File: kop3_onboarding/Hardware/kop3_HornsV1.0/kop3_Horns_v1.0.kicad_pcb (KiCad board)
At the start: 2 copper layers, 0 parts

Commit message: PCB Layout for Horn Breakout Board Done.
Created the PCB for the Horn Breakout Board.
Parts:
- added C1: 100 uF, Capacitor_SMD:C_0805_2012Metric_Pad1.18x1.45mm_HandSolder, F.Cu at (75.5, 63.0)
- added C10: C, Capacitor_SMD:C_0805_2012Metric_Pad1.18x1.45mm_HandSolder, F.Cu at (75.5, 44.9)
- added C11: .01 uF, Capacitor_SMD:C_0805_2012Metric_Pad1.18x1.45mm_HandSolder, F.Cu at (75.5, 41.9)
- added C12: .01 uF, Capacitor_SMD:C_0805_2012Metric_Pad1.18x1.45mm_HandSolder, F.Cu at (75.5, 38.9)
- added C2: .01 uF, Capacitor_SMD:C_0805_2012Metric_Pad1.18x1.45mm_HandSolder, F.Cu at (75.5, 60.0)
- added C4: 10 uF, Capacitor_SMD:C_0805_2012Metric_Pad1.18x1.45mm_HandSolder, F.Cu at (75.5, 57.0)
- added C5: 10 uF, Capacitor_SMD:C_0805_2012Metric_Pad1.18x1.45mm_HandSolder, F.Cu at (75.5, 54.0)
- added C6: 1 uF, Capacitor_SMD:C_0805_2012Metric_Pad1.18x1.45mm_HandSolder, F.Cu at (75.5, 51.0)
- added C7: 1 uF, Capacitor_SMD:C_0805_2012Metric_Pad1.18x1.45mm_HandSolder, F.Cu at (75.5, 48.0)
- added D2: S2JTR, Diode_SMD:D_SMB, F.Cu at (99.0, 53.8)
- added F1: 2A, Fuse:Fuse_0805_2012Metric_Pad1.15x1.40mm_HandSolder, F.Cu at (100.2, 47.5)
- added J1: Power, Connector_Molex:Molex_KK-254_AE-6410-03A_1x03_P2.54mm_Vertical, F.Cu at (86.8, 63.3)
- added J2: HORN_CONTROL, Connector_Molex:Molex_KK-254_AE-6410-02A_1x02_P2.54mm_Vertical, F.Cu at (81.7, 40.8)
- added J3: HORN_OUT1, Connector_Molex:Molex_KK-254_AE-6410-02A_1x02_P2.54mm_Vertical, F.Cu at (89.5, 40.8)
- added J4: HORN_OUT2, Connector_Molex:Molex_KK-254_AE-6410-02A_1x02_P2.54mm_Vertical, F.Cu at (96.5, 40.8)
- added Q1: IRF540N, Package_TO_SOT_THT:TO-220-3_Vertical, F.Cu at (93.0, 51.3)
- added R1: 1K, Resistor_THT:R_Axial_DIN0204_L3.6mm_D1.6mm_P5.08mm_Horizontal, F.Cu at (83.0, 54.0)
- added REF**: MountingHole_3.2mm_M3, MountingHole:MountingHole_3.2mm_M3, F.Cu at (99.8, 70.2)
- added REF**: MountingHole_3.2mm_M3, MountingHole:MountingHole_3.2mm_M3, F.Cu at (77.0, 32.5)
- added SW1: SW_Push, Button_Switch_SMD:SW_Push_1P1T_NO_6x6mm_H9.5mm, F.Cu at (96.3, 61.8)
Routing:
- net GND: track 0.00 -> 47.8 mm, vias 0 -> 1
- net +24V: track 0.00 -> 37.2 mm
- net /HORN_CONTROL: track 0.00 -> 30.5 mm
- net Net-(D2-K): track 0.00 -> 21.2 mm
- net Net-(J4-Pin_2): track 0.00 -> 6.21 mm
- net Net-(J3-Pin_2): track 0.00 -> 4.45 mm
- net Net-(D2-A): track 0.00 -> 3.59 mm
- added copper zone on F.Cu, net +24V
- added copper zone on B.Cu, net GND
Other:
- board outline added: 33.1 x 48.6 mm

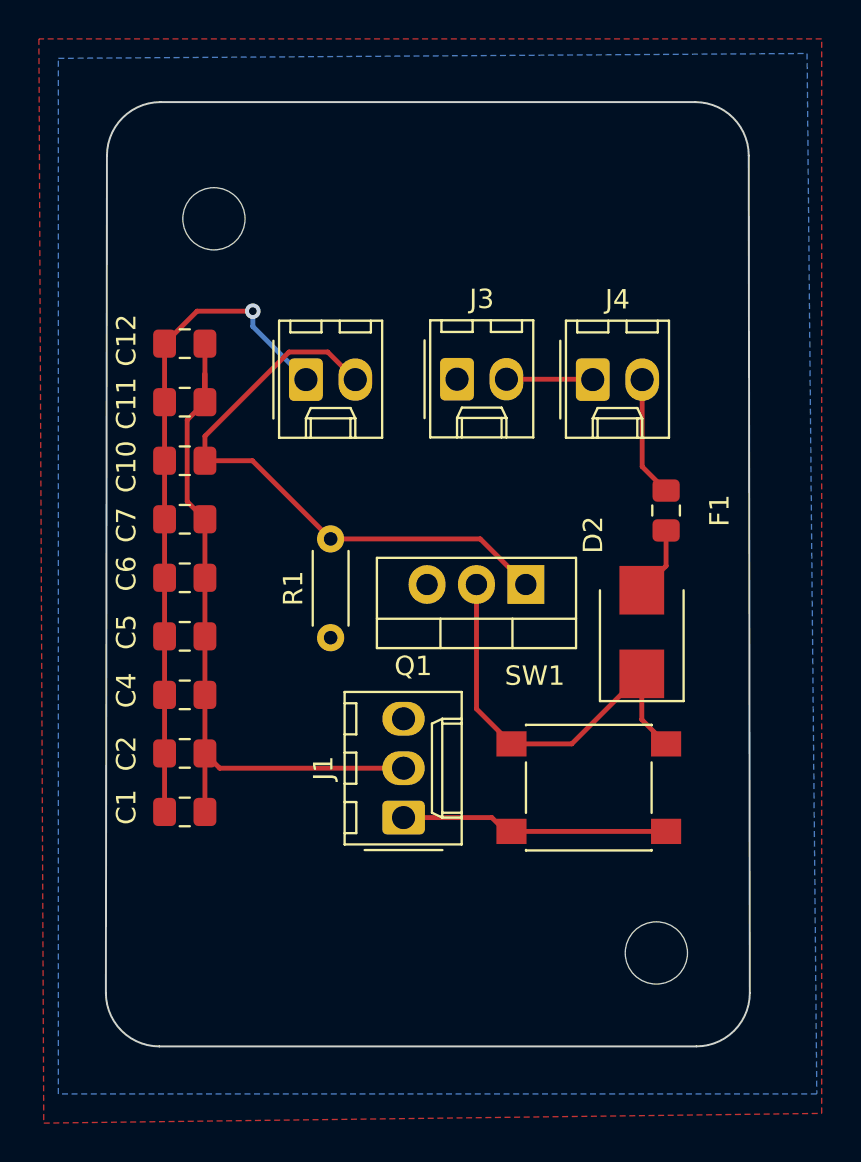
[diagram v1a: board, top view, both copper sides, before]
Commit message: Onboarding Check FIX
Switched the connector footprints, and rearranged the rectifier diode to protect against current back flow and from high current flowing through the mosfet/tripping the fuse. Re-arranged the PCB layout.
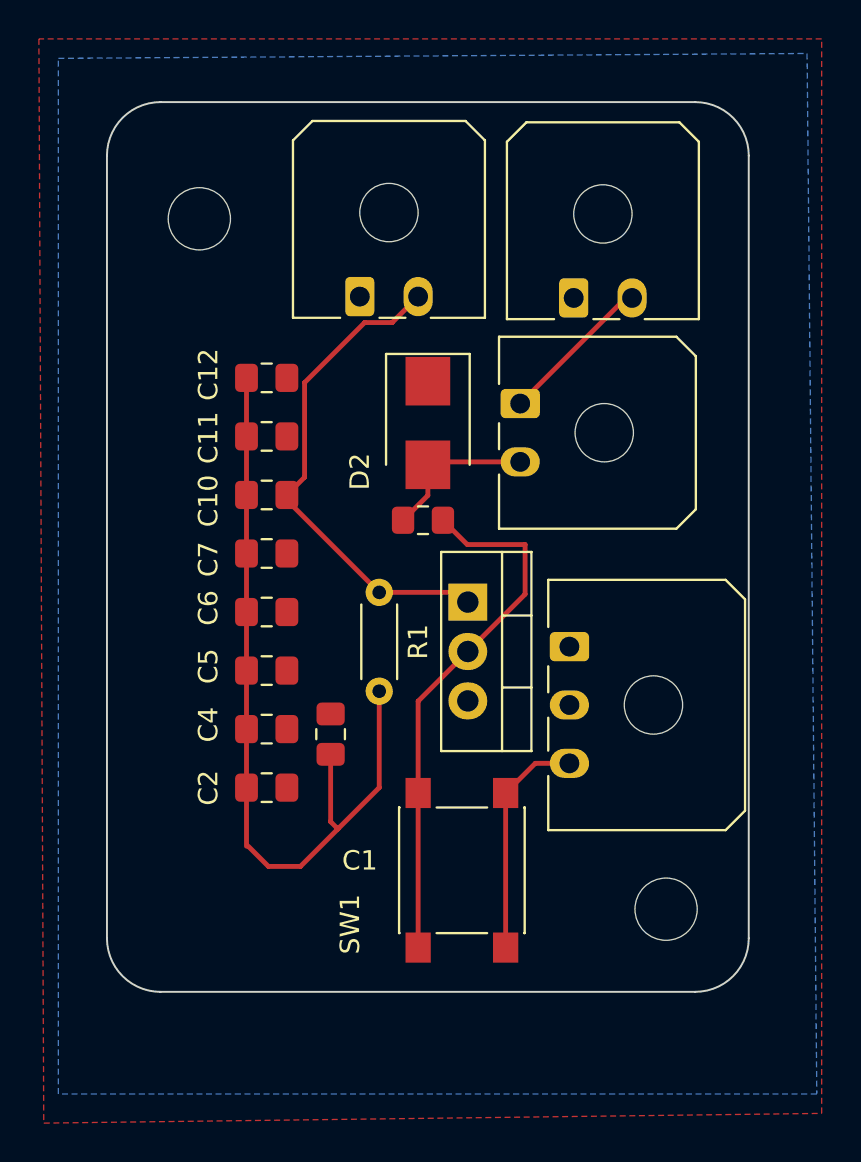
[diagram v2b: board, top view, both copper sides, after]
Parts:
- C10: value C -> .1 uF
- J1: footprint Connector_Molex:Molex_KK-254_AE-6410-03A_1x03_P2.54mm_Vertical -> Connector_Molex:Molex_Micro-Fit_3.0_43650-0300_1x03_P3.00mm_Horizontal
- J2, J3, J4: footprint Connector_Molex:Molex_KK-254_AE-6410-02A_1x02_P2.54mm_Vertical -> Connector_Molex:Molex_Micro-Fit_3.0_43650-0200_1x02_P3.00mm_Horizontal
- moved D2 15.4 mm to (88.0, 43.0), turned to -90 degrees
- moved F1 12.5 mm to (87.8, 48.0), turned to 0 degrees
- moved J1 12.2 mm to (95.3, 54.5), turned to -90 degrees
- moved C1 8.50 mm to (83.0, 59.0), turned to -90 degrees
- moved SW1 7.79 mm to (89.8, 66.0), turned to 90 degrees
- moved J3 7.31 mm to (95.5, 36.6)
- moved J2 5.09 mm to (84.5, 36.5)
- moved C10 4.57 mm to (79.7, 46.7)
- moved C4 4.57 mm to (79.7, 58.7)
- moved C11 4.57 mm to (79.7, 43.7)
- moved C12 4.57 mm to (79.7, 40.7)
- moved C2 4.57 mm to (79.7, 61.8)
- moved C5 4.57 mm to (79.7, 55.7)
- moved C6 4.57 mm to (79.7, 52.7)
- moved C7 4.57 mm to (79.7, 49.7)
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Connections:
- D2 pad 1: Net-(D2-K) -> +24V
- F1 pad 1: Net-(J4-Pin_2) -> Net-(D2-A)
- F1 pad 2: Net-(D2-A) -> Net-(Q1-D)
- J4 pad 2: Net-(J4-Pin_2) -> Net-(D2-A)
- Q1 pad 2: Net-(D2-K) -> Net-(Q1-D)
- SW1 pad 1: Net-(D2-K) -> Net-(Q1-D)
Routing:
- net +24V: track 37.2 -> 0.37 mm
- net Net-(Q1-D): track 0.00 -> 27.8 mm
- net Net-(D2-K): track 21.2 -> 0.00 mm
- net Net-(J4-Pin_2): track 6.21 -> 0.00 mm
- net GND: track 47.8 -> 53.9 mm, vias 1 -> 0
- net /HORN_CONTROL: track 30.5 -> 25.6 mm
- net Net-(D2-A): track 3.59 -> 8.19 mm
- net Net-(J3-Pin_2): track 4.45 -> 8.00 mm
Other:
- board size 33.1 x 48.6 mm -> 33 x 45.8 mm
